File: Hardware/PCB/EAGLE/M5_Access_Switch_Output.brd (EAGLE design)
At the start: 20.2 x 36 mm, 11 parts, among them K1 G3VM-41AY1, K2 G3VM-41AY1

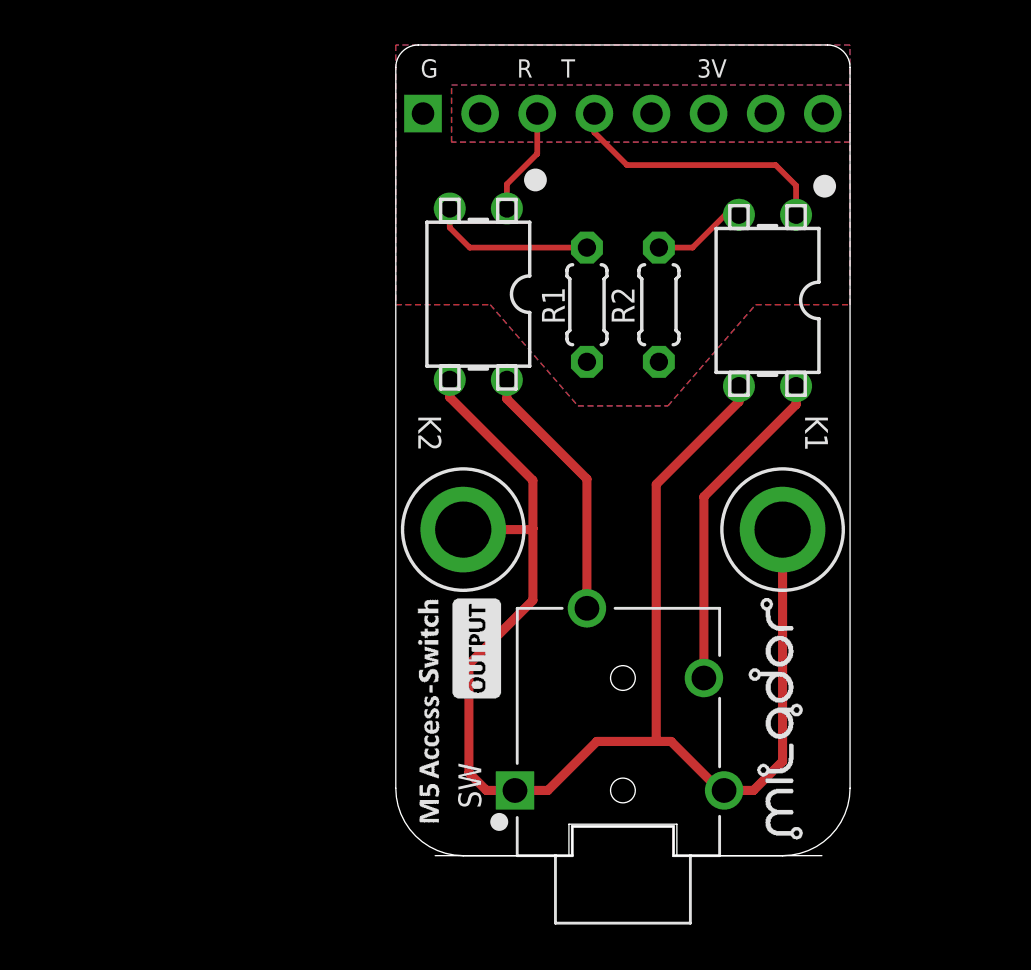
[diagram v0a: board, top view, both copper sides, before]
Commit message: Updated design to two mono jack design
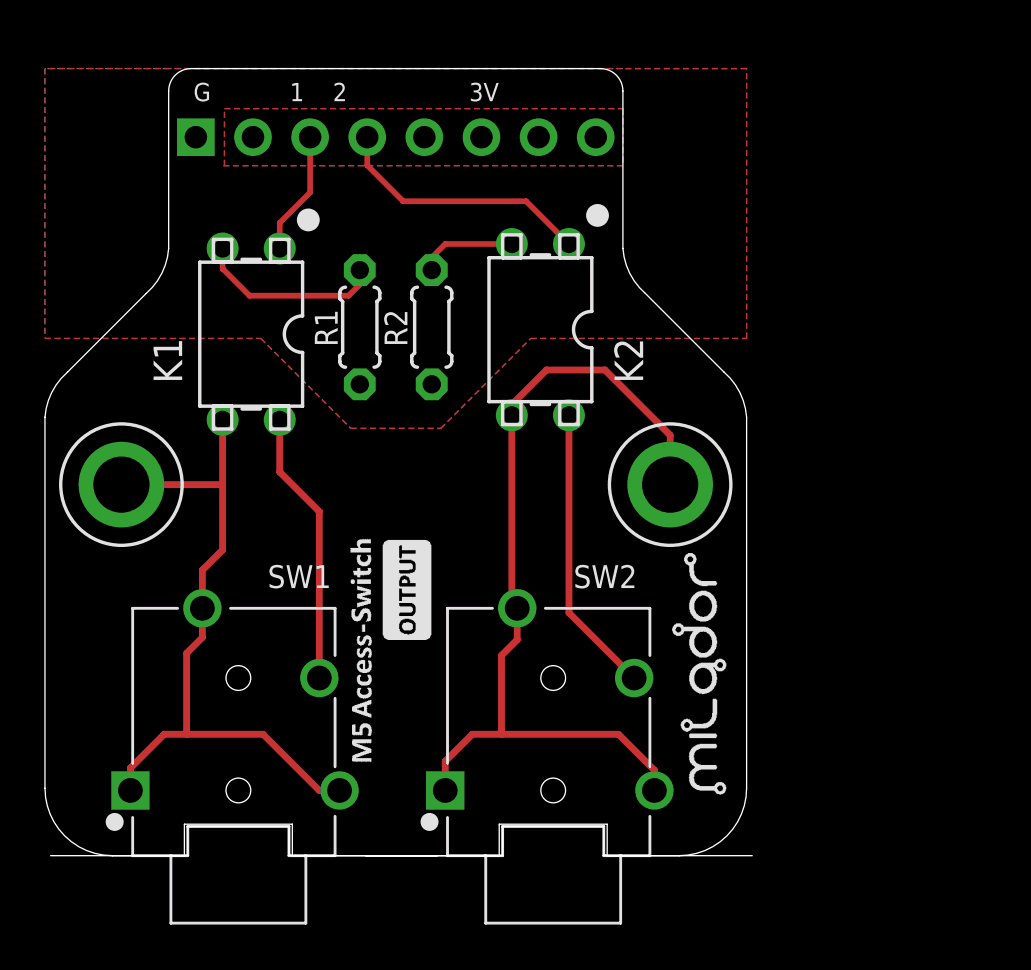
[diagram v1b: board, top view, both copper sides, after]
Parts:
- removed SW: SJ-43514, milador:CUI_SJ-43514
- added SW1, SW2: SJ-43514, milador:CUI_SJ-43514
- moved K1 23.0 mm to (-5.16, 27.0)
- moved H1 15.3 mm to (-12.2, 16.5)
- moved JP1 10.2 mm to (0.00, 31.9)
- moved R1 10.1 mm to (-1.60, 23.5)
- moved R2 10.1 mm to (1.60, 23.5)
- moved H2 5.39 mm to (12.2, 16.5)
- moved LABEL_OUTPUT_TOP 4.05 mm to (0.50, 11.8)
- moved LABEL_DEVICE_TOP 4.04 mm to (-1.40, 9.10)
- moved LABEL_LOGO_TOP 3.94 mm to (14.0, 7.40)
- moved K2 3.18 mm to (7.70, 27.2)
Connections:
- removed net N$1: K2.2, R1.2
- removed net N$4: K1.2, R2.2
- removed net OUT-COMMON-PIN: H1.P1, H2.P1, K1.3, K2.3, SW.1, SW.4
- new net +3V3: JP1.7
- new net N$2: K2.2, R2.2
- new net N$3: K1.2, R1.2
- new net OUT1-COMMON-PIN: H1.P1, K1.3, SW1.1, SW1.3, SW1.4
- new net OUT2-COMMON-PIN: H2.P1, K2.3, SW2.1, SW2.3, SW2.4
- net OUT-1-PIN: now also K2.4, SW2.2; no longer K1.4, SW.2
- net OUT-2-PIN: now also K1.4, SW1.2; no longer K2.4, SW.3
- net SWITCH_1_PIN: now also JP1.3; no longer JP1.4
- net SWITCH_2_PIN: now also JP1.4; no longer JP1.3
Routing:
- net OUT-COMMON-PIN: track 67.5 -> 0.00 mm
- net OUT2-COMMON-PIN: track 0.00 -> 38.8 mm
- net OUT1-COMMON-PIN: track 0.00 -> 31.1 mm
- net N$3: track 0.00 -> 8.34 mm
- net N$1: track 7.32 -> 0.00 mm
- net SWITCH_2_PIN: track 4.78 -> 11.7 mm
- net SWITCH_1_PIN: track 12.1 -> 5.51 mm
- net N$2: track 0.00 -> 4.37 mm
- net N$4: track 4.16 -> 0.00 mm
- net OUT-1-PIN: track 14.7 -> 12.9 mm
- net OUT-2-PIN: track 11.6 -> 12.2 mm
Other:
- board size 20.2 x 36 mm -> 31.2 x 35 mm
- board text added: "G 1 2 3V"
- board text removed: "G R T 3V"
- board text removed: "R"
